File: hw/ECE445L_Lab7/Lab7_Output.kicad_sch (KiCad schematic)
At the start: 14 parts, among them J4 AudioJack, U16 Adafruit ST7735R

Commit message: Final PCB commit
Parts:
- added D5: POWER, ECE445L:LED_D5.0mm, symbol ECE445L:LED
- added Q13, Q14, Q15, Q16, Q17, Q18: MMBF170, Package_TO_SOT_SMD:SOT-23, symbol Transistor_FET:MMBF170
- added R100, R106: 125, Resistor_SMD:R_0603_1608Metric_Pad0.98x0.95mm_HandSolder, symbol Device:R
- added R101, R107: 100, Resistor_SMD:R_0603_1608Metric_Pad0.98x0.95mm_HandSolder, symbol Device:R
- added R102, R108: 75, Resistor_SMD:R_0603_1608Metric_Pad0.98x0.95mm_HandSolder, symbol Device:R
- added R103, R104, R105, R109, R110, R111: 2k, Resistor_SMD:R_0603_1608Metric_Pad0.98x0.95mm_HandSolder, symbol Device:R
- added R99: 1.5V, Resistor_SMD:R_0603_1608Metric_Pad0.98x0.95mm_HandSolder, symbol Device:R
- D1: value LED -> PD6
- D2: value LED -> PD7
- J3: renamed from J4; footprint ECE445L:Jack_3.5mm_CUI_SJ1-3523N_Horizontal -> ECE445L:STX3000; symbol ECE445L:HeadphoneJack -> ECE445L:HeadphoneJack_STX3000
- renumbered C39 to C35, C40 to C36, R85 to R95, R86 to R96, R87 to R97, R88 to R98, TP11 to TP13, TP12 to TP14, U16 to U15
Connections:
- net +3V3: now also R99.1
- net GND: now also D5.1 (K)
- net L_AudioOut: now also R97.2, Q13.2 (S), Q14.2 (S), Q15.2 (S); no longer R96.2
- net R_AudioOut: now also R96.2, Q16.2 (S), Q17.2 (S), Q18.2 (S); no longer R97.2
- new net: Q17.3 (D), R107.1
- new net: Q16.3 (D), R108.1
- new net: Q13.1 (G), R103.2
- new net: D5.2 (A), R99.2
- new net: Q18.1 (G), R111.2
- new net: Q18.3 (D), R106.1
- new net: Q13.3 (D), R102.1
- new net: Q14.1 (G), R104.2
- new net: Q15.1 (G), R105.2
- new net: Q15.3 (D), R100.2
- new net: Q17.1 (G), R110.2
- new net: Q14.3 (D), R101.1
- new net: Q16.1 (G), R109.2
- new net L_AudioBuf: R100.1, R101.2, R102.2
- new net PC4: R103.1, R109.1
- new net PC5: R104.1, R110.1
- new net PC6: R105.1, R111.1
- new net R_AudioBuf: R106.2, R107.2, R108.2

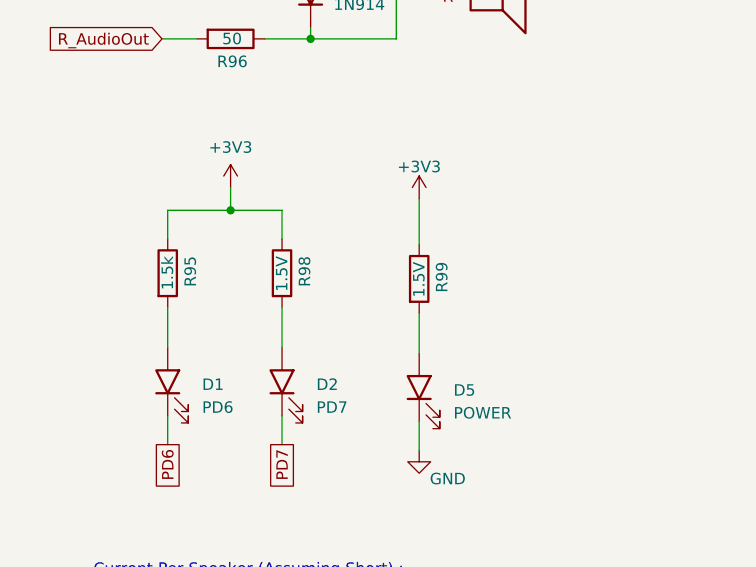
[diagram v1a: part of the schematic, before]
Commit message: Updated bom for lab 7B
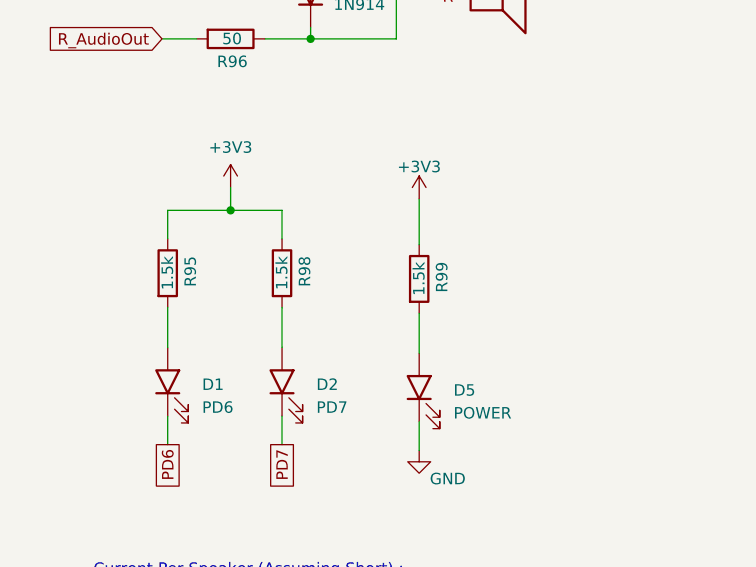
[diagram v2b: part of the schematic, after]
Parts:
- R98, R99: value 1.5V -> 1.5k
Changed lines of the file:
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@@
 			)
 		)
-		(property "Value" "1.5V"
+		(property "Value" "1.5k"
 			(at 59.69 79.375 90)
 			(effects
@@
 			)
 		)
-		(property "Value" "1.5V"
+		(property "Value" "1.5k"
 			(at 44.45 78.74 90)
 			(effects
